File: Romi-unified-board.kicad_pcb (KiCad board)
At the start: 4 copper layers, 125.1 x 125.8 mm, 67 parts, among them J1 ServoAnalog, J10 LIDAR_DATA, J11 LIDAR_MOTOR, J12 ROMI-Encoder, J13 ROMI-Encoder, J14 THING, J15 THING, J2 Conn_01x19_Female, J3 LineSensor, J4 LineSensor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

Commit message: back traces away from holes.
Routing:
- net GPIO13: track 116.5 -> 118.5 mm, vias 10 -> 8
- net GPIO17: track 189.6 -> 190.8 mm
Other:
- rule pad_to_mask_clearance: 0.01 -> 0.001

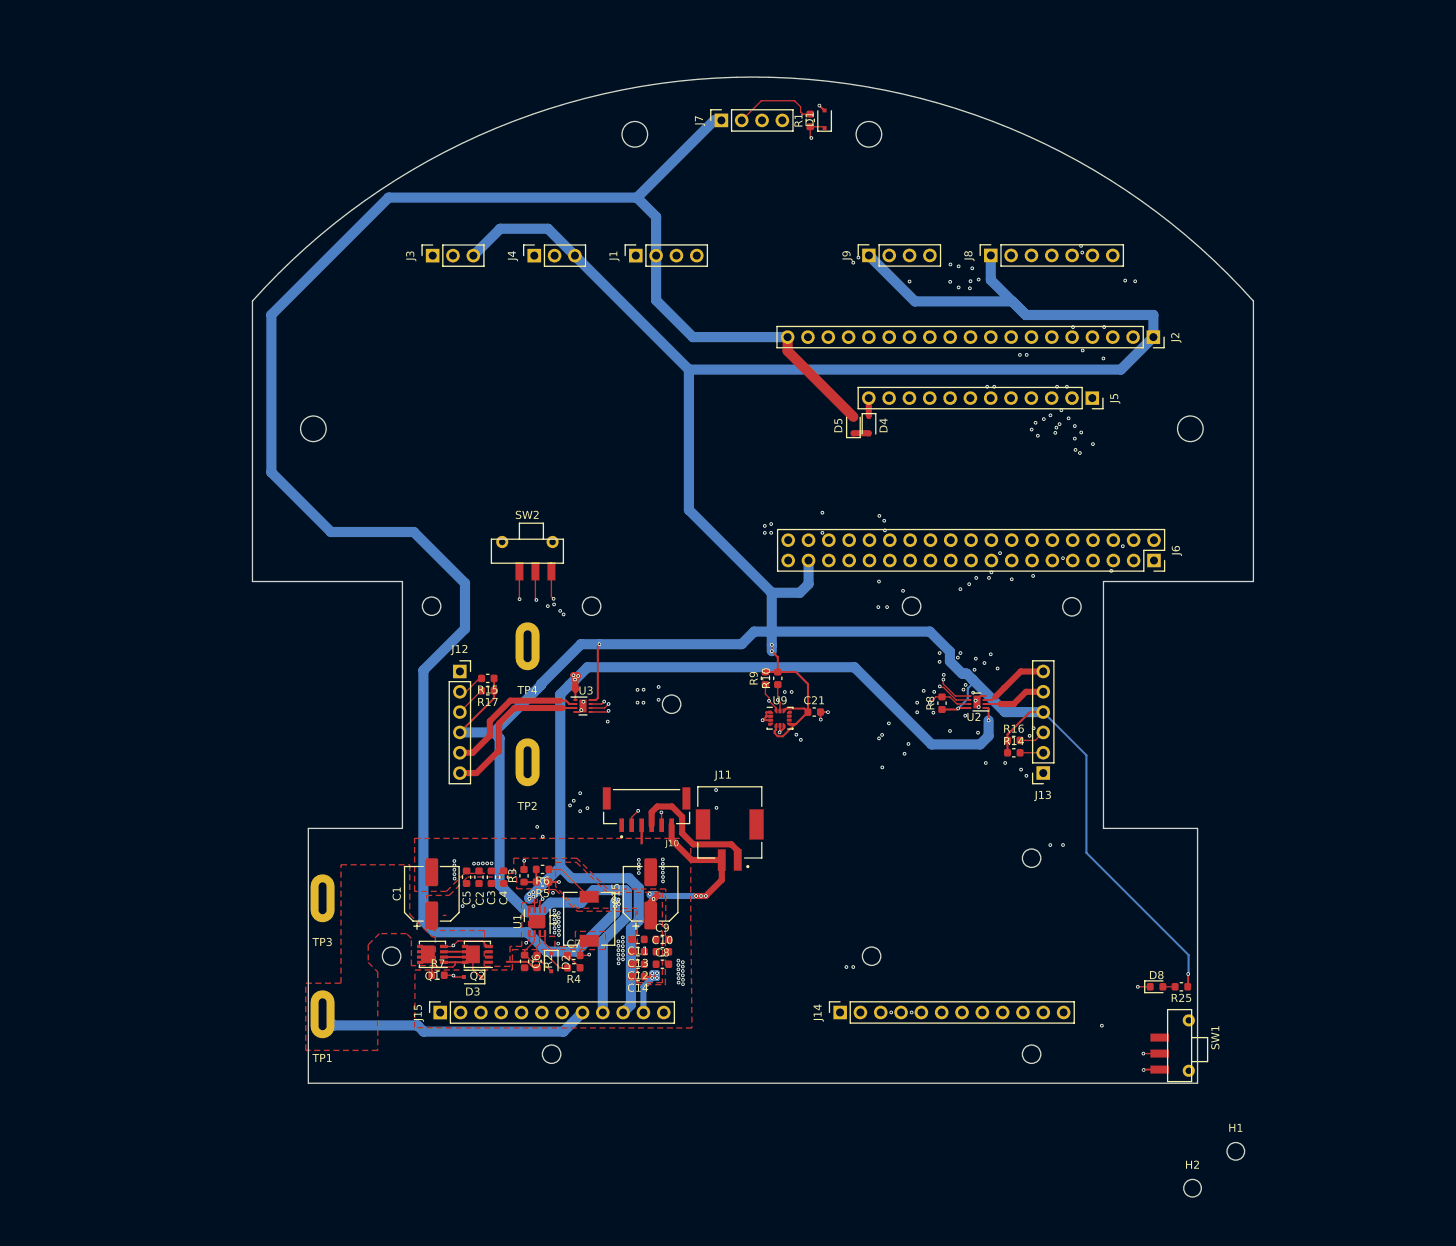
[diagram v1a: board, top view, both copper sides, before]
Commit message: flipped ultrasonic, removed IO2 from j8
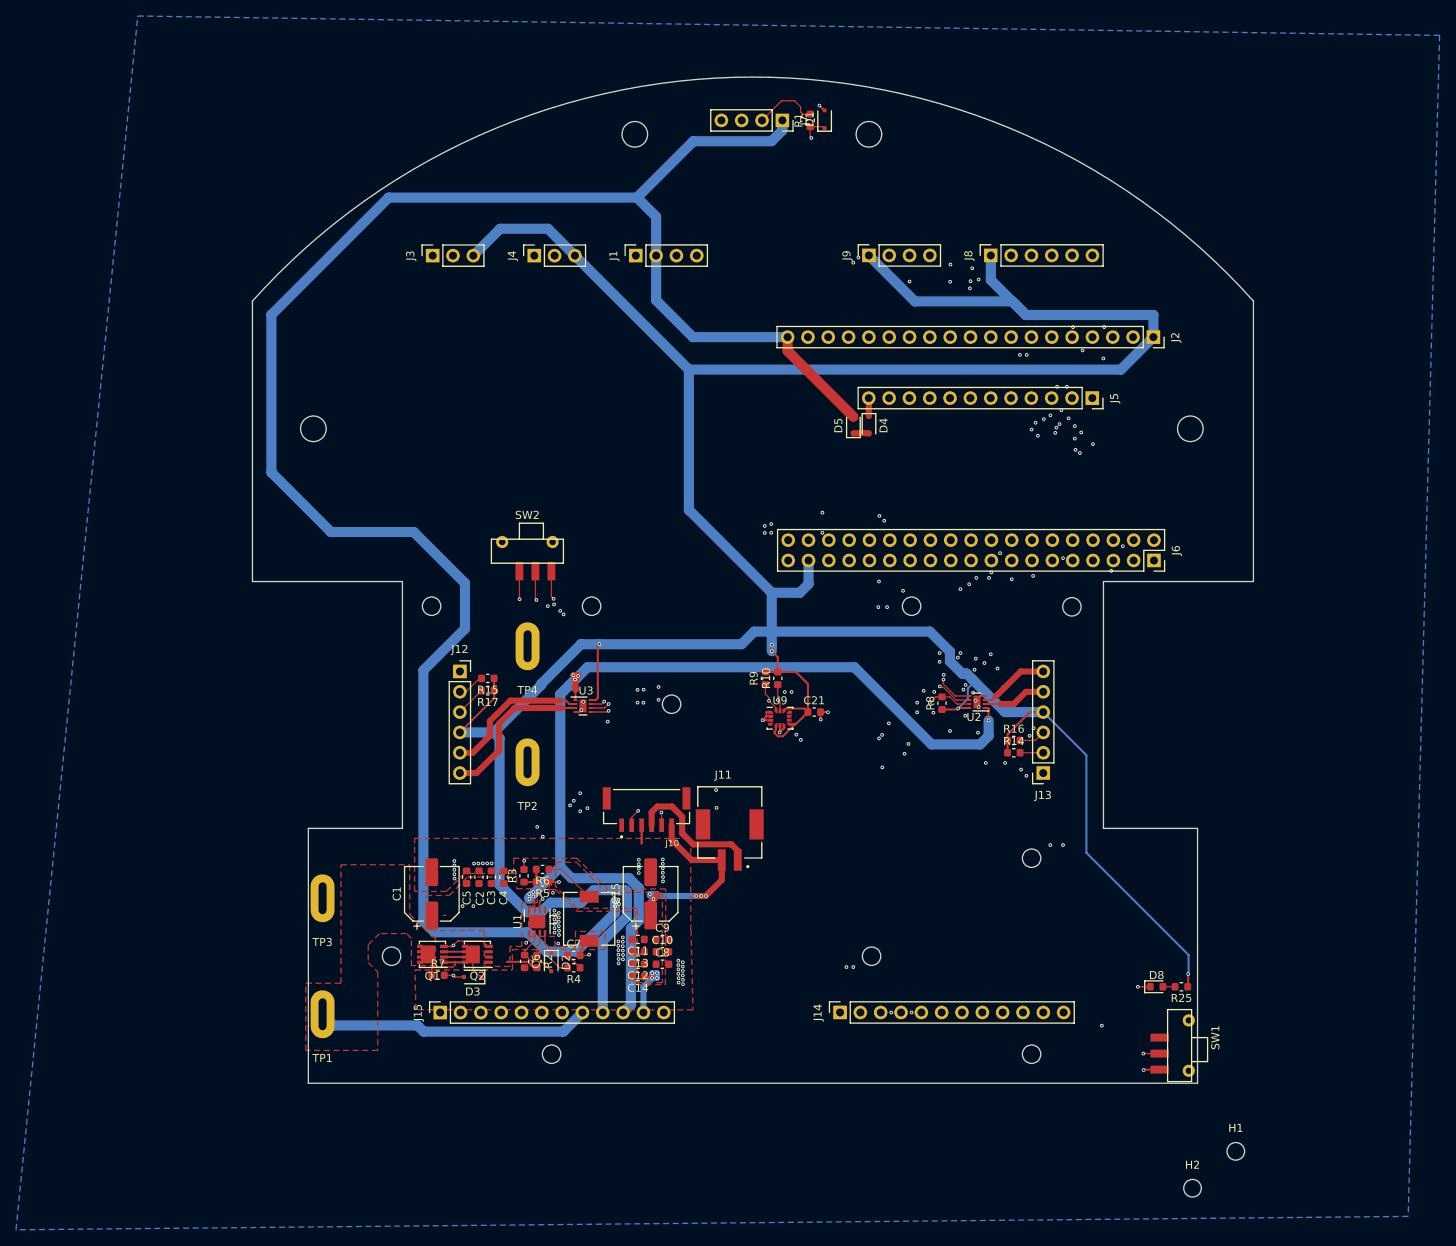
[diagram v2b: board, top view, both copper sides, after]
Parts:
- J8: footprint Connector_PinSocket_2.54mm:PinSocket_1x07_P2.54mm_Vertical -> Connector_PinSocket_2.54mm:PinSocket_1x06_P2.54mm_Vertical
- moved J7 7.62 mm to (122.8, 35.5), turned to 270 degrees
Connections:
- J8 pad 6: GPIO2 -> GND
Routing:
- net GPIO2: track 64.3 -> 0.00 mm, vias 7 -> 0
- net +5V: track 286.0 -> 294.3 mm
- net GPIO17: track 190.8 -> 195.1 mm, vias 11 -> 9
- net Net-(J7-Pad2): track 10.6 -> 8.10 mm
- net GPIO19: track 125.0 -> 123.3 mm
- added copper zone on B.Cu, net GND

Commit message: Added silk.
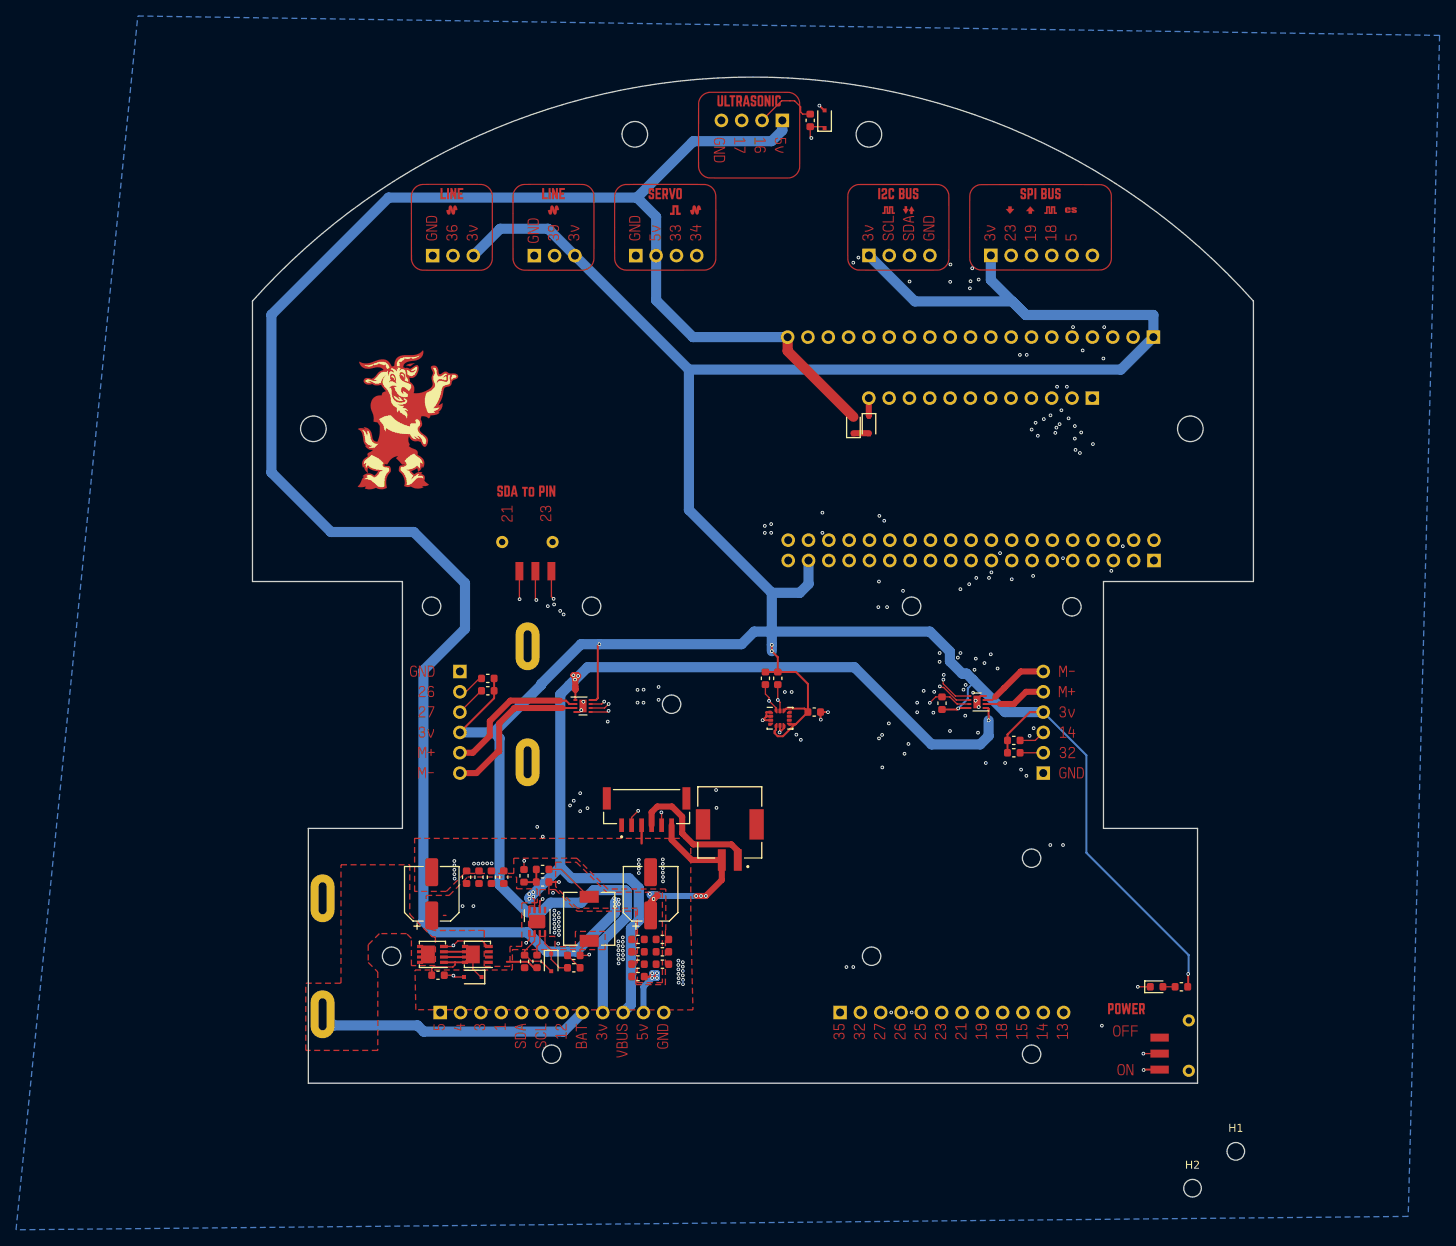
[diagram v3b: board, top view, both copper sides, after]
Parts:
- added Ref**: Val**, unified:Romi-unified-board-F_Cu, F.Cu at (119.0, 93.0)

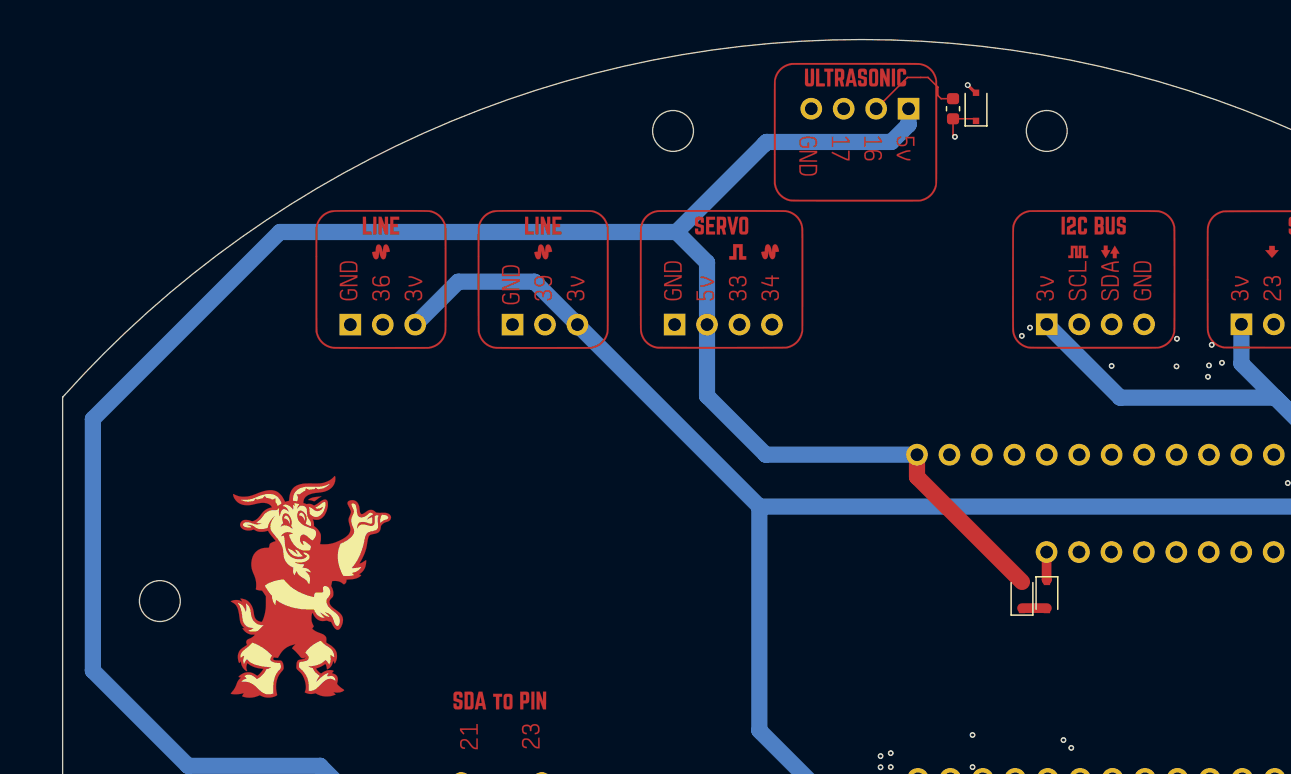
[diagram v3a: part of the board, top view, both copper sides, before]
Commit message: Fixed DRC errors, generated gerbers.
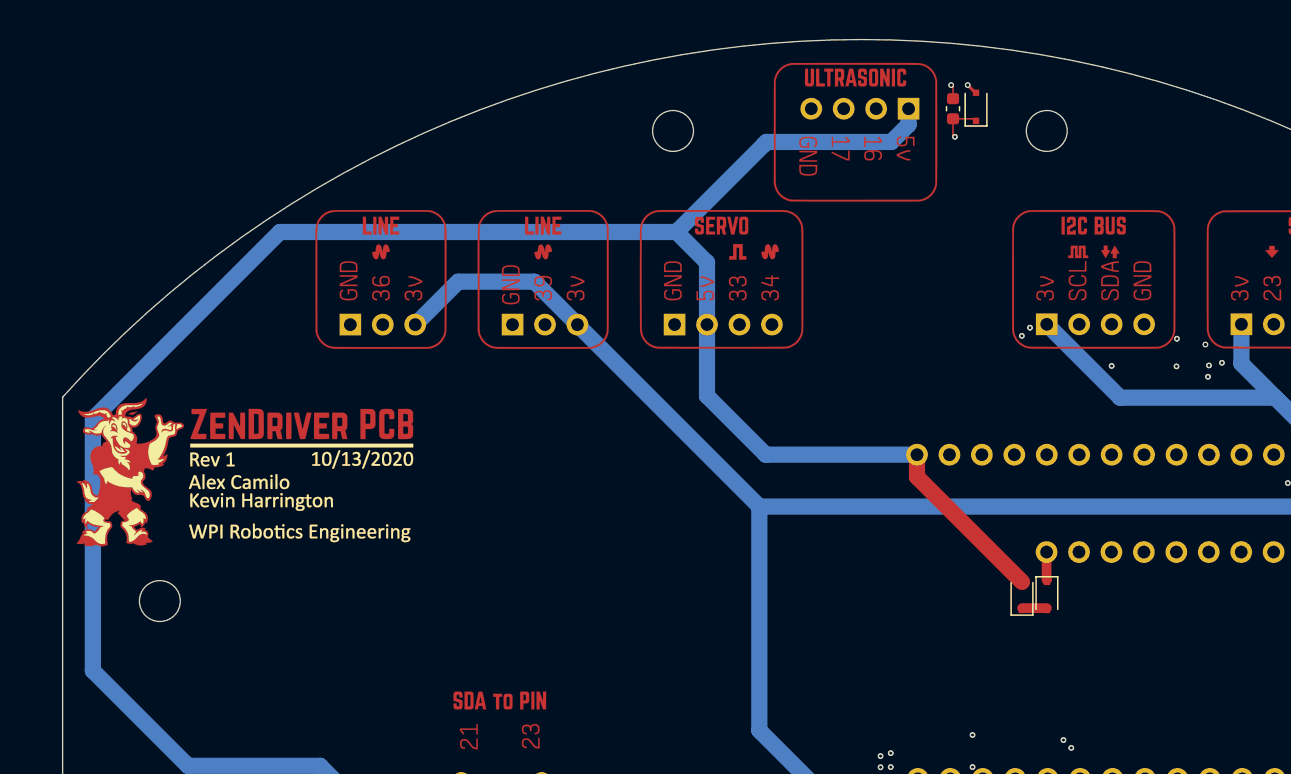
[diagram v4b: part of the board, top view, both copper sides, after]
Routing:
- net GPIO23: track 197.3 -> 198.7 mm
- net Net-(J7-Pad2): track 8.10 -> 7.76 mm, vias 0 -> 1
